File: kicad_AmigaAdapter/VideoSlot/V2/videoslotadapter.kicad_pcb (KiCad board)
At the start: 2 copper layers, 152 x 57.6 mm, 22 parts, among them U1 74LVC86, U2 74LVC574, U3 74LVC574, U4 TLV74333PDBVR, U5 74LVC86

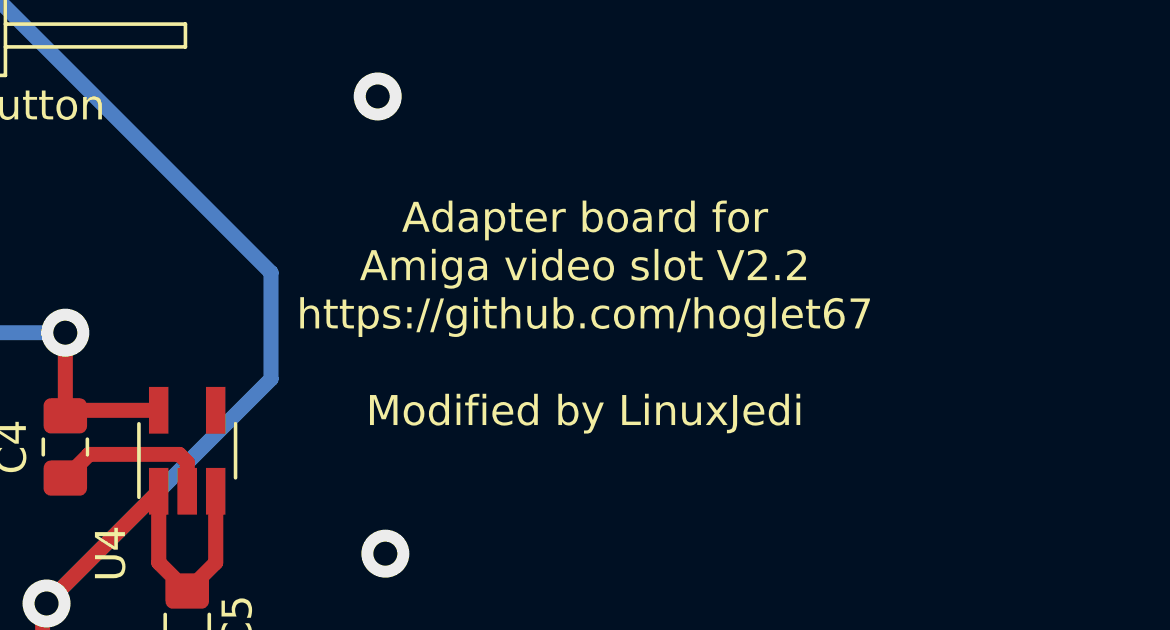
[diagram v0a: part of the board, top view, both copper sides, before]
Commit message: Remove LinuxJedi from silks
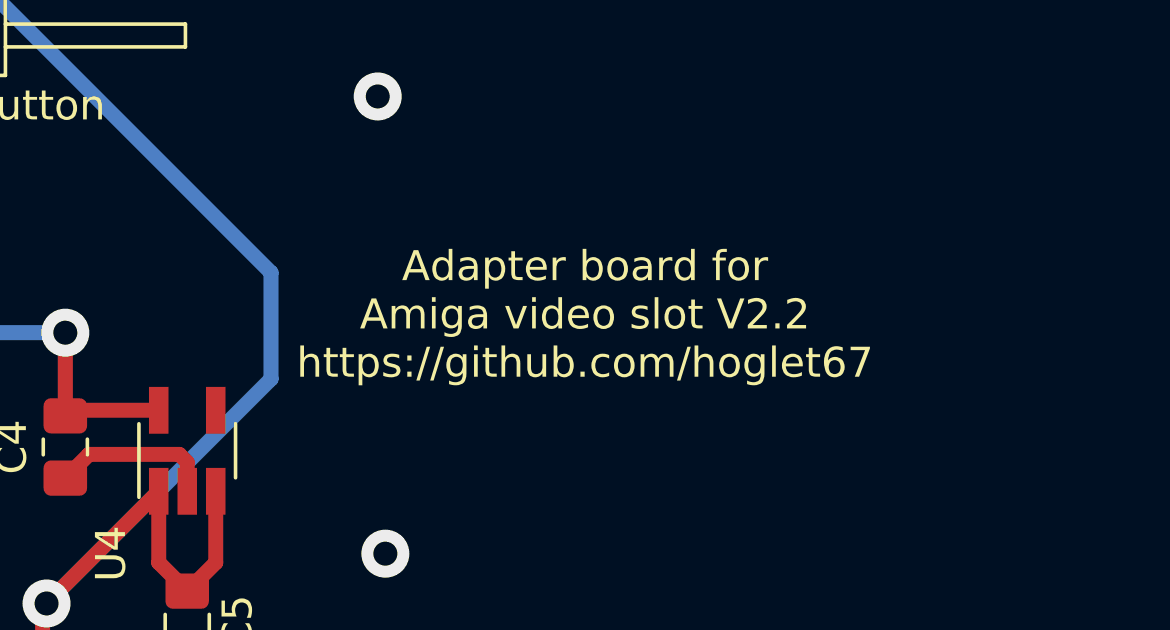
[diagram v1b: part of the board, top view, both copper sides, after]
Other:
- board text added: "Adapter board for Amiga video slot V2.2 https://github.com/hoglet67"
- board text removed: "Adapter board for Amiga video slot V2.2 https://github.com/hoglet67 Modified by LinuxJedi"
